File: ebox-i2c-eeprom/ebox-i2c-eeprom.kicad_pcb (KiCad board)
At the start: 2 copper layers, 45 x 75 mm, 10 parts, among them J1 xconch_pinheader_2x40, J2 xconch_pinsocket_2x40, U1 AT24C64

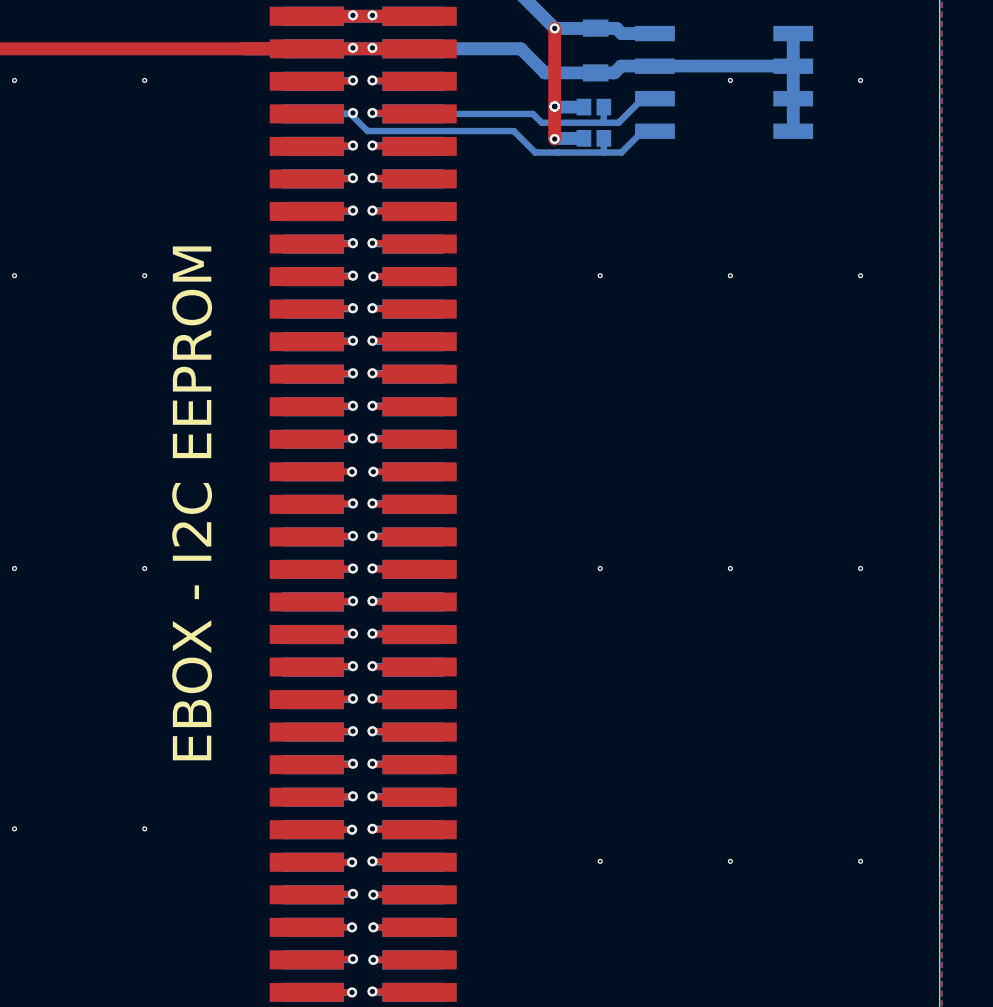
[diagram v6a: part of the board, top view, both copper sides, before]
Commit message: add logo for some pcb
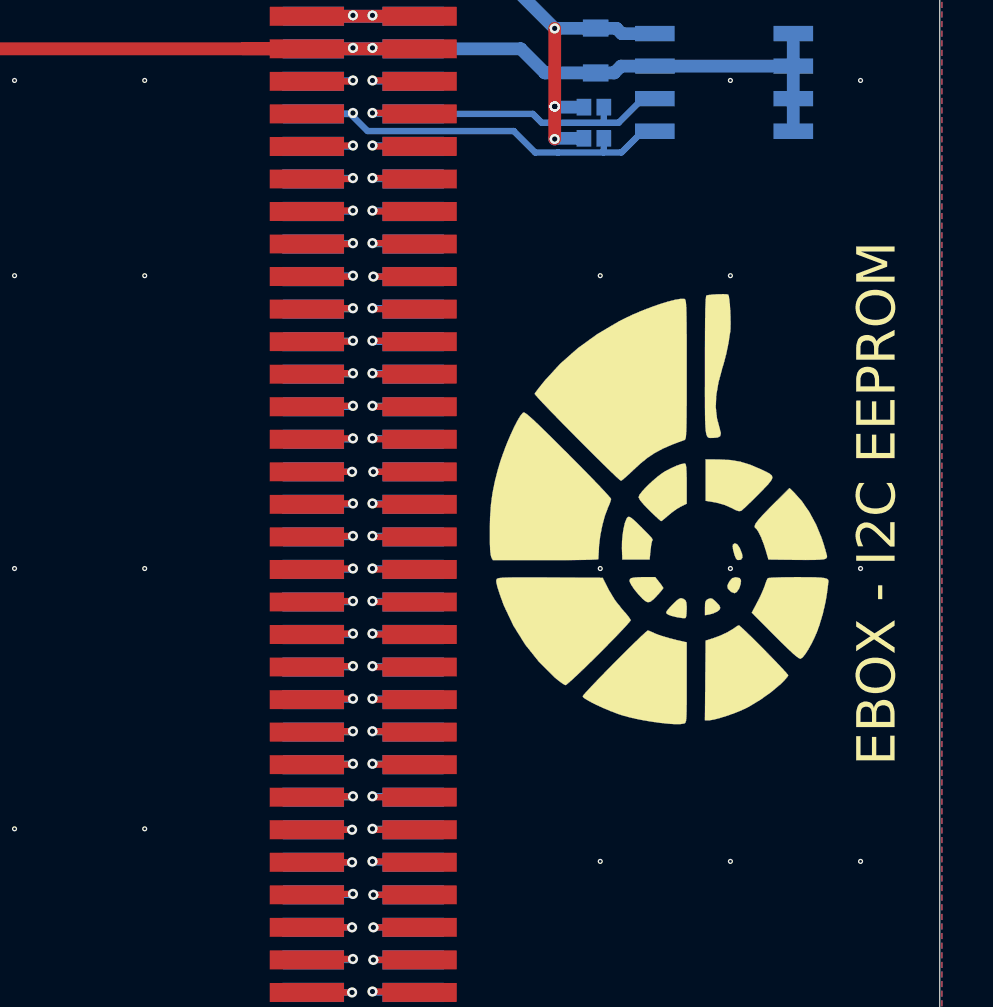
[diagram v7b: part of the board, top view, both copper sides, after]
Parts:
- added ?: , xconch:xconch_logo, F.Cu at (35.6, 39.4)
